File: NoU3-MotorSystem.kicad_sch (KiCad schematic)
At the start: 40 parts, among them J1 JST SR/SZ, J10 JST SR/SZ, J13 JST SR/SZ, J15 Barrel_Jack, J16 VIN, J17 JST SR/SZ, J18 GND, J19 JST SR/SZ, J4 JST SR/SZ, J7 JST SR/SZ, Q1 AO3401A, U10 PCA9685BS, U15 SY8113BADC, U16 SY8113BADC, U8 5.8 ZSPT

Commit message: Panel updates for next production run, removed version sns
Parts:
- J1, J10, J13, J17, J19, J4: LCSC C160392 -> C3029336
- J7: LCSC C3029336 -> C3029336
- L1, L2: LCSC C98354 -> C88528
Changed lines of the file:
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@@
 			)
 		)
-		(property "Datasheet" "https://jlcpcb.com/partdetail/171772-BM06B_SRSS_TB_LF_SN/C160392"
+		(property "Datasheet" ""
 			(at 243.84 66.04 0)
 			(hide yes)
@@
 			)
 		)
-		(property "LCSC" "C160392"
+		(property "LCSC" "C3029336 "
 			(at 243.84 66.04 0)
 			(hide yes)
@@
 			)
 		)
-		(property "Datasheet" "https://jlcpcb.com/partdetail/171772-BM06B_SRSS_TB_LF_SN/C160392"
+		(property "Datasheet" ""
 			(at 237.49 124.46 0)
 			(hide yes)
@@
 			)
 		)
-		(property "LCSC" "C160392"
+		(property "LCSC" "C3029336 "
 			(at 237.49 124.46 0)
 			(hide yes)
@@
 			)
 		)
-		(property "Datasheet" "https://jlcpcb.com/partdetail/171772-BM06B_SRSS_TB_LF_SN/C160392"
+		(property "Datasheet" ""
 			(at 265.43 124.46 0)
 			(hide yes)
@@
 			)
 		)
-		(property "LCSC" "C160392"
+		(property "LCSC" "C3029336 "
 			(at 265.43 124.46 0)
 			(hide yes)
@@
 			)
 		)
-		(property "Datasheet" "https://jlcpcb.com/partdetail/171772-BM06B_SRSS_TB_LF_SN/C160392"
+		(property "Datasheet" ""
 			(at 237.49 39.37 0)
 			(hide yes)
@@
 			)
 		)
-		(property "LCSC" "C160392"
+		(property "LCSC" "C3029336 "
 			(at 237.49 39.37 0)
 			(hide yes)
@@
 			)
 		)
-		(property "LCSC" "C3029336"
+		(property "LCSC" "C3029336 "
 			(at 237.49 97.79 0)
 			(hide yes)
@@
 			)
 		)
-		(property "Datasheet" "https://jlcpcb.com/partdetail/171772-BM06B_SRSS_TB_LF_SN/C160392"
+		(property "Datasheet" ""
 			(at 265.43 97.79 0)
 			(hide yes)
@@
 			)
 		)
-		(property "LCSC" "C160392"
+		(property "LCSC" "C3029336 "
 			(at 265.43 97.79 0)
 			(hide yes)
@@
 			)
 		)
-		(property "Datasheet" "https://jlcpcb.com/partdetail/171772-BM06B_SRSS_TB_LF_SN/C160392"
+		(property "Datasheet" ""
 			(at 274.32 66.04 0)
 			(hide yes)
@@
 			)
 		)
-		(property "LCSC" "C160392"
+		(property "LCSC" "C3029336 "
 			(at 274.32 66.04 0)
 			(hide yes)
@@
 			)
 		)
-		(property "Datasheet" "https://www.lcsc.com/product-detail/Power-Inductors_Sunlord-Sunlord-WPN252012H4R7MT_C98354.html"
+		(property "Datasheet" ""
 			(at 66.04 171.45 0)
 			(hide yes)
@@
 			)
 		)
-		(property "LCSC" "C98354"
+		(property "LCSC" "C88528"
 			(at 66.04 171.45 0)
 			(hide yes)
@@
 			)
 		)
-		(property "Datasheet" "https://www.lcsc.com/product-detail/Power-Inductors_Sunlord-Sunlord-WPN252012H4R7MT_C98354.html"
+		(property "Datasheet" ""
 			(at 66.04 140.97 0)
 			(hide yes)
@@
 			)
 		)
-		(property "LCSC" "C98354"
+		(property "LCSC" "C88528"
 			(at 66.04 140.97 0)
 			(hide yes)

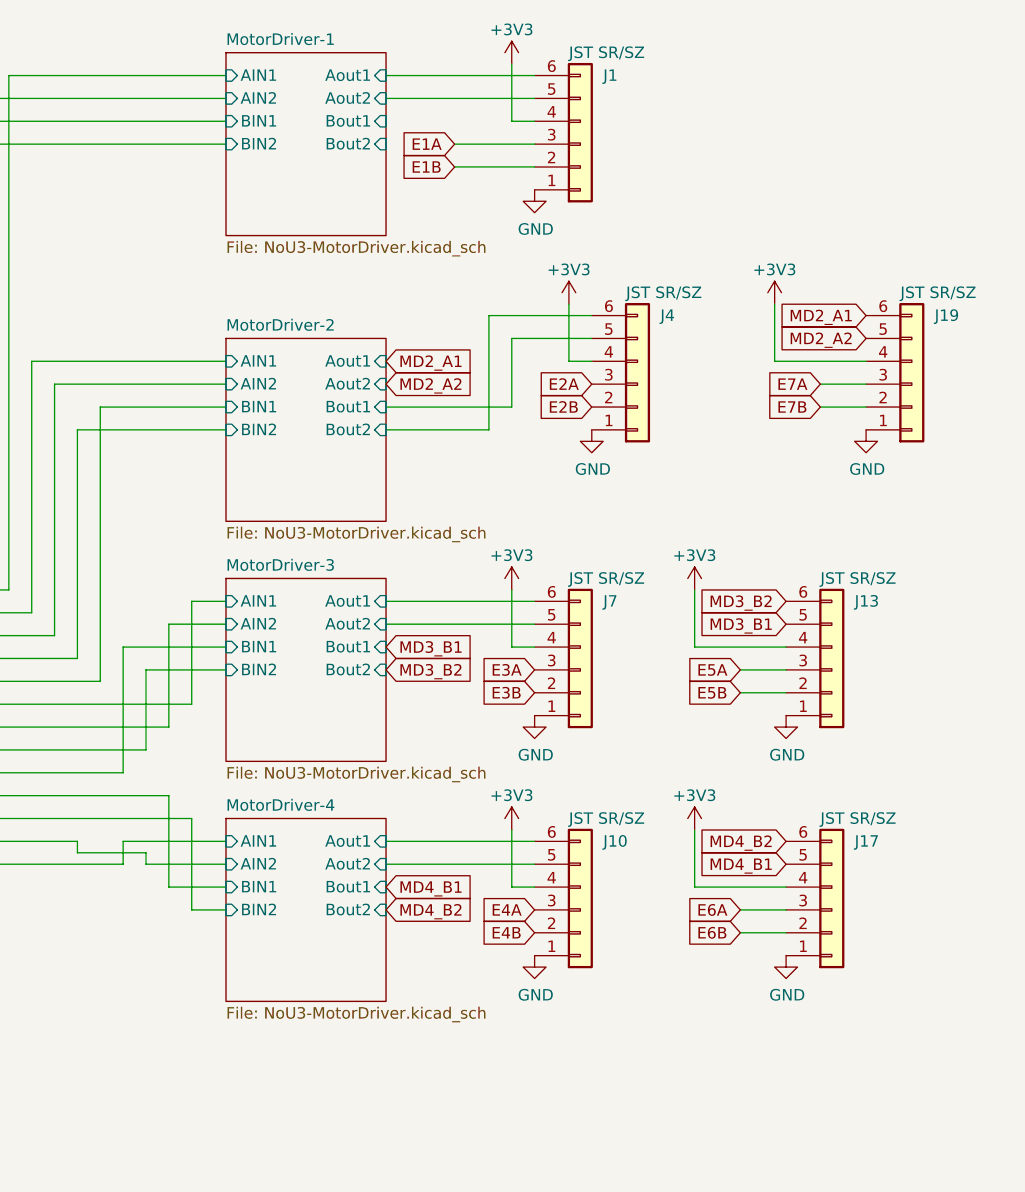
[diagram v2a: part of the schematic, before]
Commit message: cleaned up JSTs on motor driver sheet
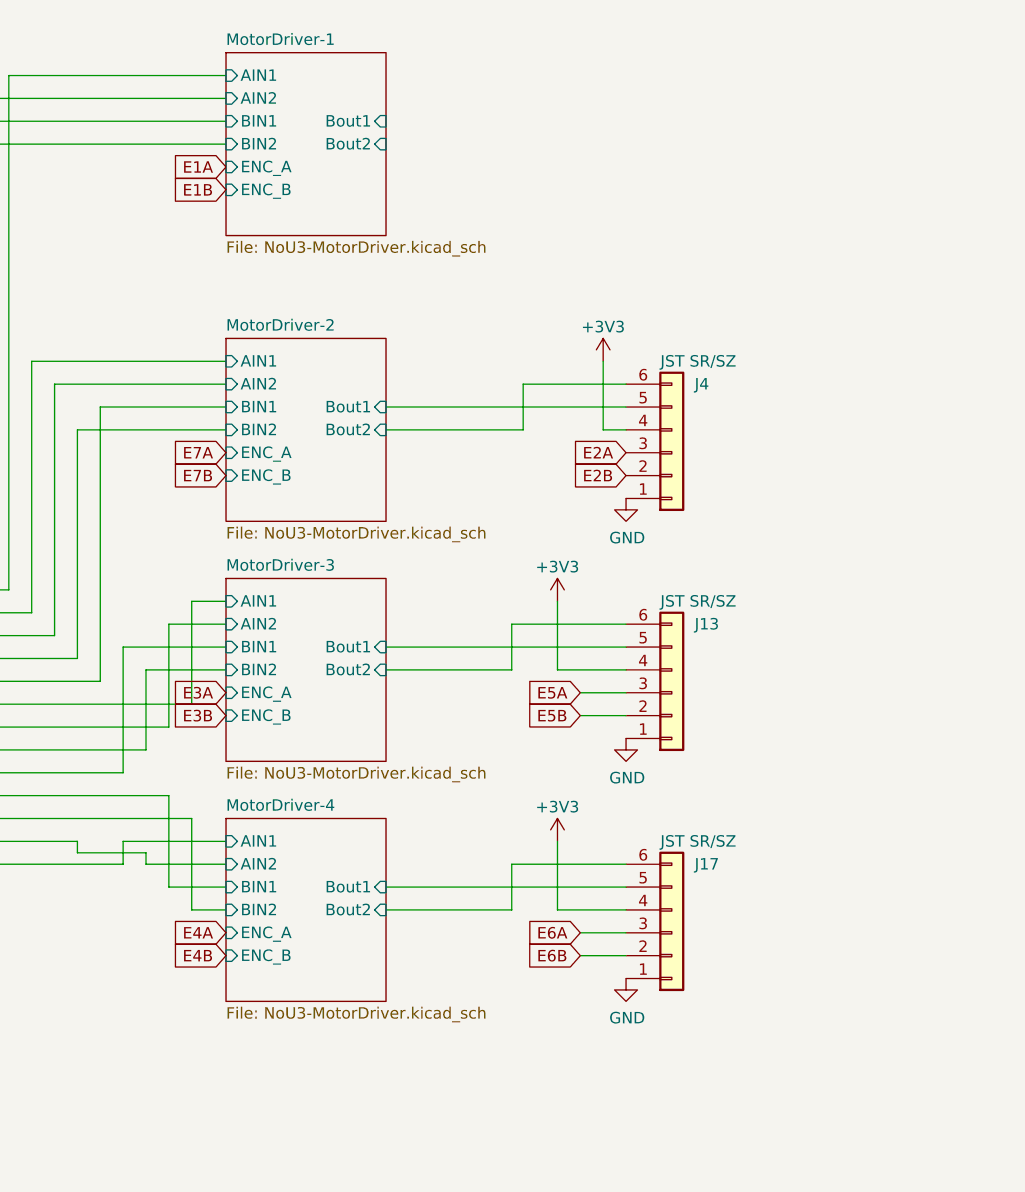
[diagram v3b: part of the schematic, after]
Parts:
- removed J1, J10, J19, J7: JST SR/SZ, AlfredoFootprints:JST_SH_1x06_Vertical, symbol Connector_Generic:Conn_01x06
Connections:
- net MD3_B1 renamed MotorDriver-3/Bout1
- net MD3_B2 renamed MotorDriver-3/Bout2
- net MD4_B1 renamed MotorDriver-4/Bout1
- net MD4_B2 renamed MotorDriver-4/Bout2
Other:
- sheet MotorDriver-1 ports: added ENC_A, ENC_B; removed Aout1, Aout2
- sheet MotorDriver-2 ports: added ENC_A, ENC_B; removed Aout1, Aout2
- sheet MotorDriver-3 ports: added ENC_A, ENC_B; removed Aout1, Aout2
- sheet MotorDriver-4 ports: added ENC_A, ENC_B; removed Aout1, Aout2
- moved on the sheet: J13, J17, J4

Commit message: first push with NoU3.7 features
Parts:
- removed J13, J17, J4: JST SR/SZ, AlfredoFootprints:JST_SH_1x06_Vertical, symbol Connector_Generic:Conn_01x06
- removed Q1: AO3401A, AlfredoFootprints:SOT-23-small, symbol Transistor_FET:AO3401A
- removed R23: 10K, Resistor_SMD:R_0402_1005Metric, symbol Device:R
- removed TP4: ECLK, AlfredoFootprints:PogoPad1, symbol Connector:TestPoint
- removed TP5: LED0, AlfredoFootprints:PogoPad1, symbol Connector:TestPoint
- removed TP6: SCL, AlfredoFootprints:PogoPad1, symbol Connector:TestPoint
- removed TP7: SDA, AlfredoFootprints:PogoPad1, symbol Connector:TestPoint
- removed TP8: MOE, AlfredoFootprints:PogoPad1, symbol Connector:TestPoint
- removed TP9: GND, AlfredoFootprints:PogoPad1, symbol Connector:TestPoint
- removed U10: PCA9685BS, Package_DFN_QFN:QFN-28-1EP_6x6mm_P0.65mm_EP4.25x4.25mm, symbol Driver_LED:PCA9685BS
- added Q2: AONR21357, Package_DFN_QFN:DFN-8-1EP_3x3mm_P0.65mm_EP1.55x2.4mm, symbol Alfredo_Symbols:AONR21357
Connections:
- net VCC: now also Q2.1 (S), Q2.2 (S), Q2.3 (S)
- net at U8.2: now also Q2.5 (D), Q2.6 (D), Q2.7 (D), Q2.8 (D), Q2.9 (D)
- net at D1.2 (A), R10.1: now also Q2.4 (G)
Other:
- added sheet NoU3-MotorMCU-PYA (NoU3-MotorMCU.kicad_sch)
- added sheet NoU3-MotorMCU-PYB (NoU3-MotorMCU.kicad_sch)
- sheet MotorDriver-1 ports: added AISEN, BISEN, ENC_A1, ENC_A2, ENC_B1, ENC_B2; removed Bout1, Bout2, ENC_A, ENC_B
- sheet MotorDriver-2 ports: added AISEN, BISEN, ENC_A1, ENC_A2, ENC_B1, ENC_B2; removed Bout1, Bout2, ENC_A, ENC_B
- sheet MotorDriver-3 ports: added AISEN, BISEN, ENC_A1, ENC_A2, ENC_B1, ENC_B2; removed Bout1, Bout2, ENC_A, ENC_B
- sheet MotorDriver-4 ports: added AISEN, BISEN, ENC_A1, ENC_A2, ENC_B1, ENC_B2; removed Bout1, Bout2, ENC_A, ENC_B

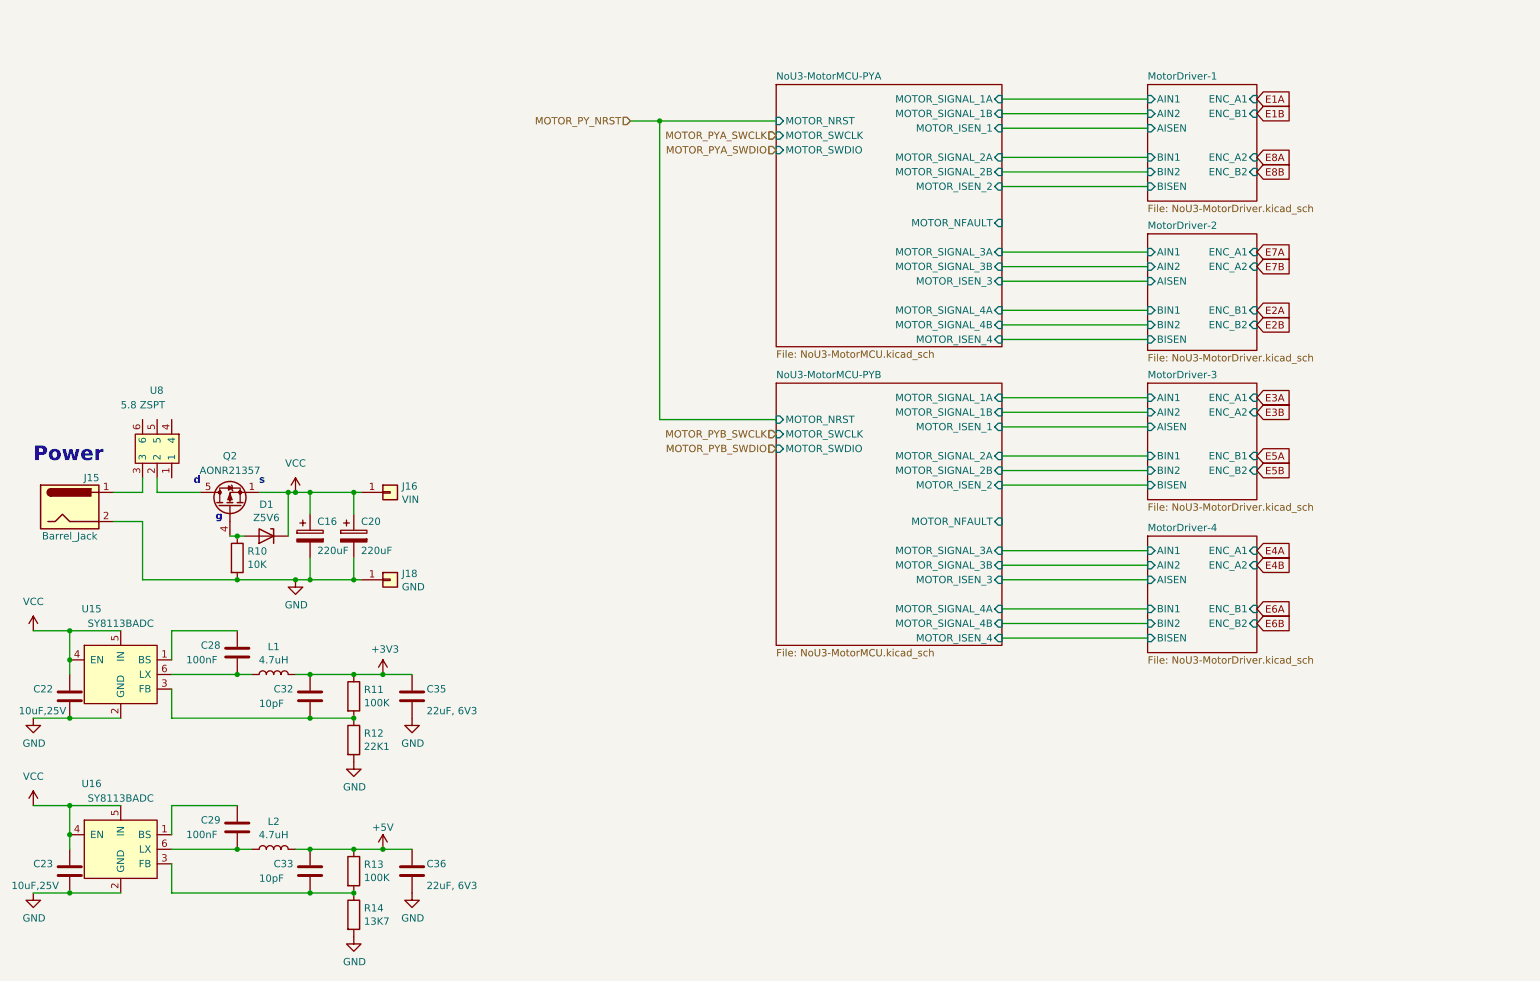
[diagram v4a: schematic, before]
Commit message: PY32F030K28U6TR motor controller chip
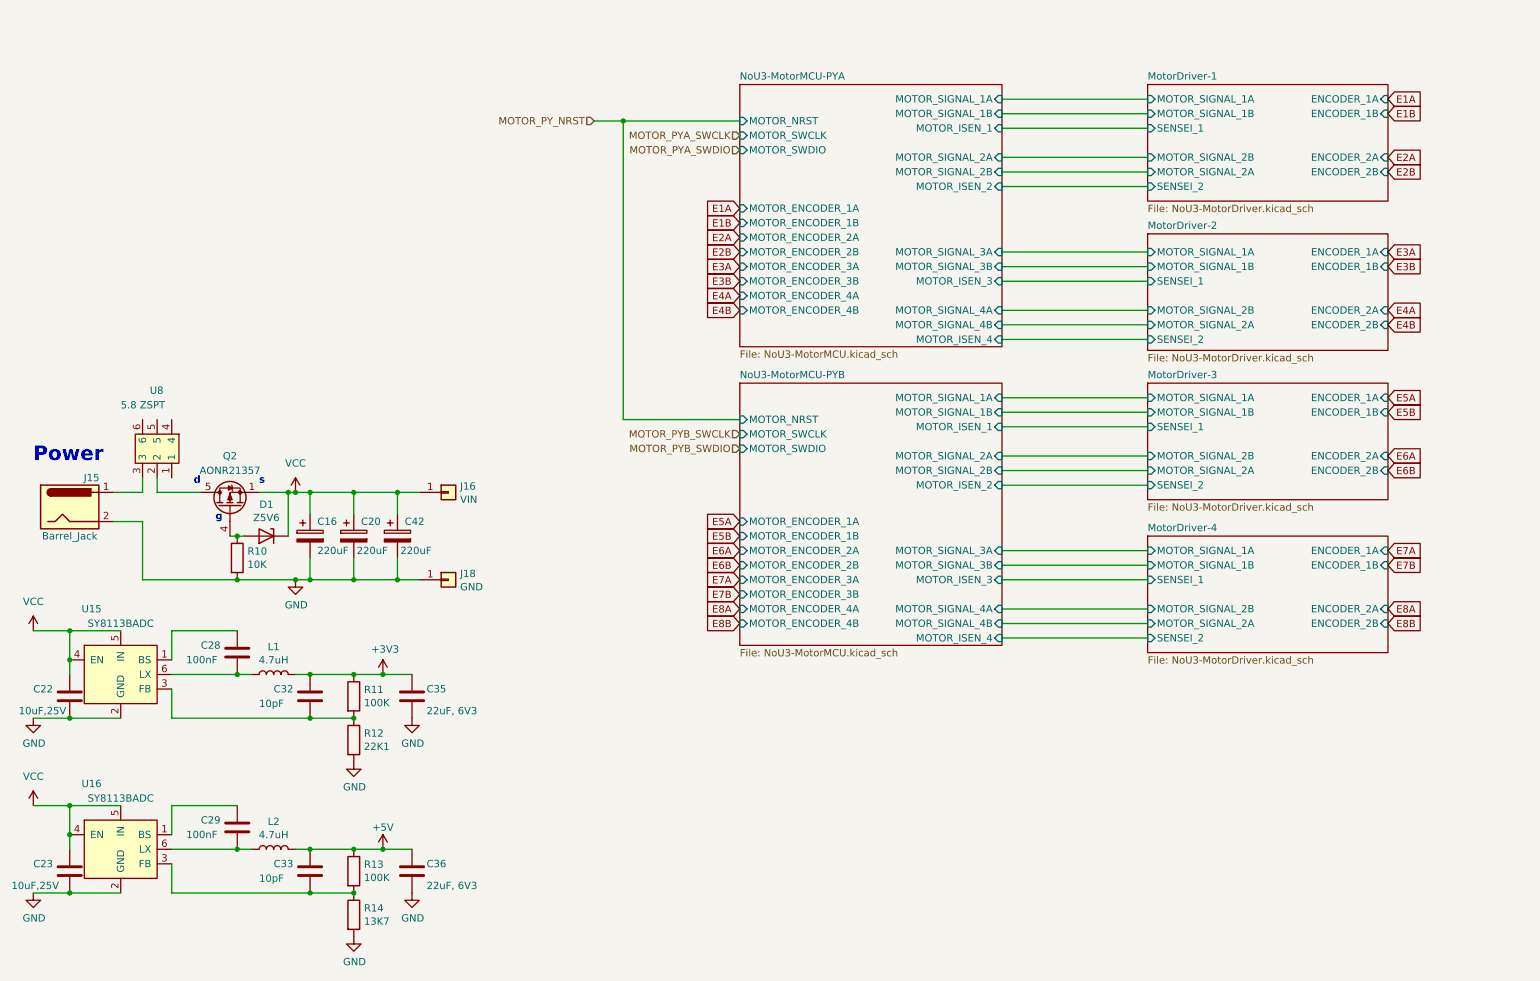
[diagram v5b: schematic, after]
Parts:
- added C42: 220uF, Capacitor_SMD:CP_Elec_6.3x7.7, symbol Device:C_Polarized
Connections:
- net GND: now also C42.2
- net VCC: now also C42.1
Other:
- sheet MotorDriver-1 ports: added ENCODER_1A, ENCODER_1B, ENCODER_2A, ENCODER_2B, MOTOR_SIGNAL_1A, MOTOR_SIGNAL_1B, MOTOR_SIGNAL_2A, MOTOR_SIGNAL_2B, SENSEI_1, SENSEI_2; removed AIN1, AIN2, AISEN, BIN1, BIN2, BISEN, ENC_A1, ENC_A2, ENC_B1, ENC_B2
- sheet MotorDriver-2 ports: added ENCODER_1A, ENCODER_1B, ENCODER_2A, ENCODER_2B, MOTOR_SIGNAL_1A, MOTOR_SIGNAL_1B, MOTOR_SIGNAL_2A, MOTOR_SIGNAL_2B, SENSEI_1, SENSEI_2; removed AIN1, AIN2, AISEN, BIN1, BIN2, BISEN, ENC_A1, ENC_A2, ENC_B1, ENC_B2
- sheet MotorDriver-3 ports: added ENCODER_1A, ENCODER_1B, ENCODER_2A, ENCODER_2B, MOTOR_SIGNAL_1A, MOTOR_SIGNAL_1B, MOTOR_SIGNAL_2A, MOTOR_SIGNAL_2B, SENSEI_1, SENSEI_2; removed AIN1, AIN2, AISEN, BIN1, BIN2, BISEN, ENC_A1, ENC_A2, ENC_B1, ENC_B2
- sheet MotorDriver-4 ports: added ENCODER_1A, ENCODER_1B, ENCODER_2A, ENCODER_2B, MOTOR_SIGNAL_1A, MOTOR_SIGNAL_1B, MOTOR_SIGNAL_2A, MOTOR_SIGNAL_2B, SENSEI_1, SENSEI_2; removed AIN1, AIN2, AISEN, BIN1, BIN2, BISEN, ENC_A1, ENC_A2, ENC_B1, ENC_B2
- sheet NoU3-MotorMCU-PYA ports: added MOTOR_ENCODER_1A, MOTOR_ENCODER_1B, MOTOR_ENCODER_2A, MOTOR_ENCODER_2B, MOTOR_ENCODER_3A, MOTOR_ENCODER_3B, MOTOR_ENCODER_4A, MOTOR_ENCODER_4B; removed MOTOR_NFAULT
- sheet NoU3-MotorMCU-PYB ports: added MOTOR_ENCODER_1A, MOTOR_ENCODER_1B, MOTOR_ENCODER_2A, MOTOR_ENCODER_2B, MOTOR_ENCODER_3A, MOTOR_ENCODER_3B, MOTOR_ENCODER_4A, MOTOR_ENCODER_4B; removed MOTOR_NFAULT
- moved on the sheet: J16, J18

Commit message: motor driver footprints
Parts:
- added C43: 220uF, AlfredoFootprints:CP_Elec_6.3x7.7_slim, symbol Device:C_Polarized
- C16, C20, C42: footprint Capacitor_SMD:CP_Elec_6.3x7.7 -> AlfredoFootprints:CP_Elec_6.3x7.7_slim
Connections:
- net GND: now also C43.2
- net VCC: now also C43.1
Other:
- moved on the sheet: J16, J18
